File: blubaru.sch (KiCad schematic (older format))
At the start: 2 parts, among them J1 DB15, J2 DB15

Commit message: Correct footprints for caps and DB15s
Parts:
- J1: footprint Connectors:DB15FC -> blubaru:DB15FC
- J2: footprint Connectors:DB15MC -> blubaru:DB15MC
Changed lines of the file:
@@
 F 0 "J2" H 6870 4850 50  0000 C CNN
 F 1 "DB15" H 6800 3150 50  0000 C CNN
-F 2 "Connectors:DB15MC" H 6850 4000 50  0001 C CNN
-F 3 "" H 6850 4000 50  0000 C CNN
+F 2 "blubaru:DB15MC" H 6850 4000 50  0001 C CNN
+F 3 "http://media.digikey.com/pdf/Data%20Sheets/Assmann%20PDFs/A-Dx%20-xx-A_KG-T4_T2_Dwg.pdf" H 6850 4000 50  0001 C CNN
 	1    6850 4000
 	1    0    0    1
@@
 F 0 "J1" H 4120 4850 50  0000 C CNN
 F 1 "DB15" H 4050 3150 50  0000 C CNN
-F 2 "Connectors:DB15FC" H 4100 4000 50  0001 C CNN
-F 3 "" H 4100 4000 50  0000 C CNN
+F 2 "blubaru:DB15FC" H 4100 4000 50  0001 C CNN
+F 3 "http://media.digikey.com/pdf/Data%20Sheets/Assmann%20PDFs/A-Dx%20-xx-A_KG-T4_T2_Dwg.pdf" H 4100 4000 50  0001 C CNN
 	1    4100 4000
 	-1   0    0    1

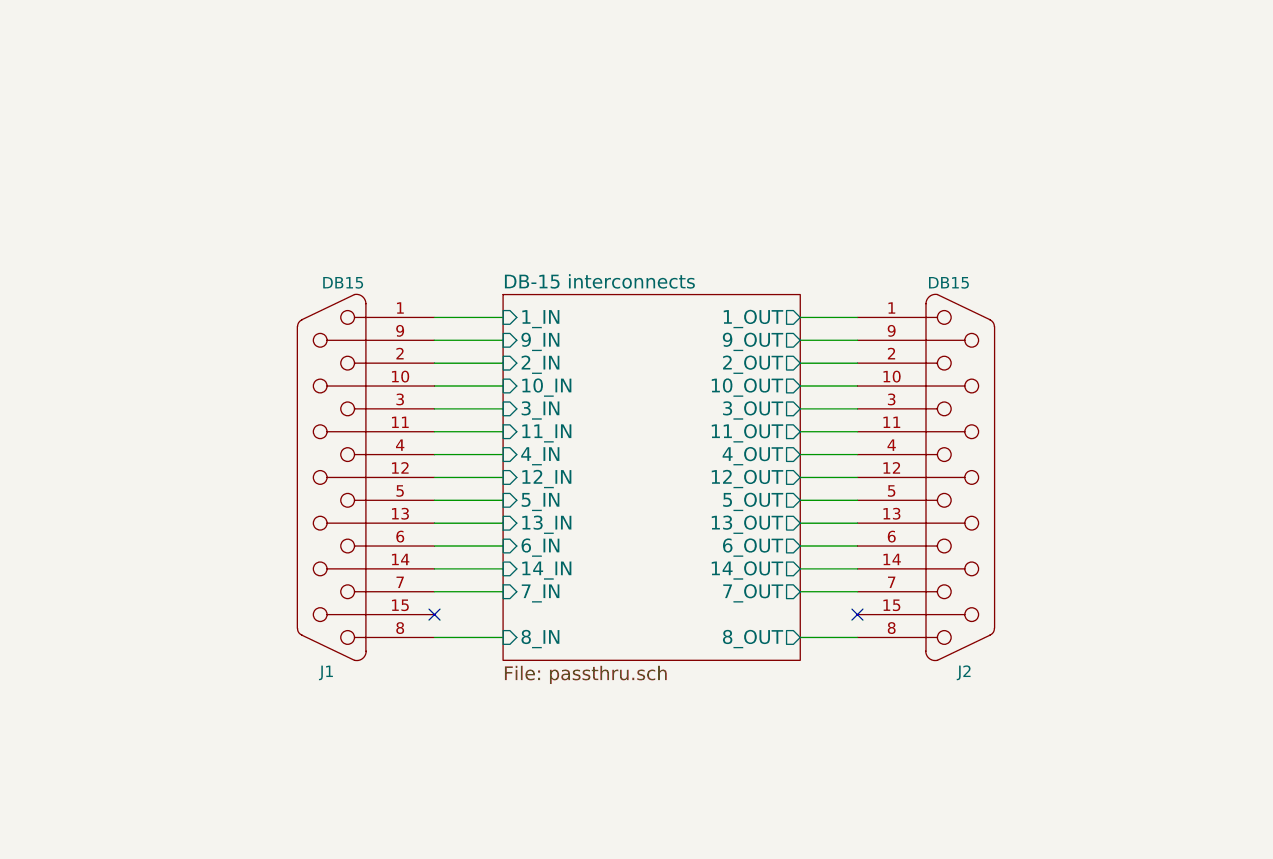
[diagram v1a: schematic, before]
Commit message: Adjust some cap prefixes and add large CD/Stereo labels to top level pages.
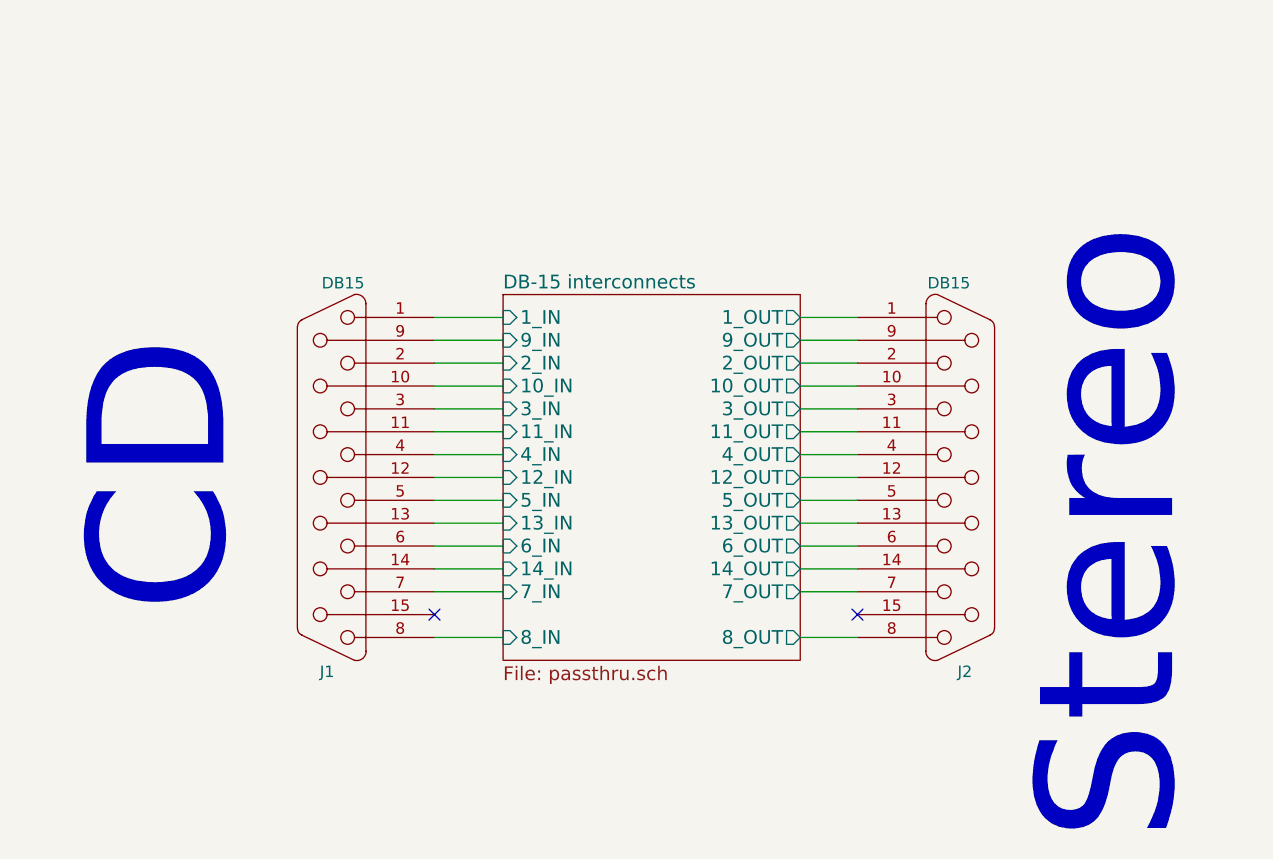
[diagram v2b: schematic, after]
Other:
- note added: "CD"
- note added: "Stereo"
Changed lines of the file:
@@
 Wire Wire Line
 	4550 4700 4850 4700
+Text Notes 3700 4600 1    600  ~ 0
+CD
+Text Notes 7850 5600 1    600  ~ 0
+Stereo
 $EndSCHEMATC
